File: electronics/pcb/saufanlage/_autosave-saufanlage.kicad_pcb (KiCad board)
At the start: 2 copper layers, 320.3 x 186.4 mm, 53 parts, among them J1 Conn_GND, J10 Conn_01x08_Male, J11 Conn_01x08_Male, J12 Conn_01x08_Male, J13 Conn_02x03_Odd_Even, J14 Conn_02x18_Odd_Even, J15 Conn_01x10_Male, J16 Conn_01x08_Male, J17 Conn_01x08_Male, J18 Conn_Finger, J19 Conn_Relais, J2 PJ-031D, J20 Conn_NFC, J21 Conn_Flow1, J22 Conn_Scale1, J23 Conn_01x15_Male, J24 Conn_01x15_Male, J25 Conn_Flow2, J26 Conn_Flow3, J27 Conn_Scale2, J28 Conn_Flow4, J29 Conn_01x15_Male, J3 Conn_3V3, J30 Conn_01x15_Male, J31 Conn_01x15_Male, J32 Conn_01x15_Male, J33 Conn_7SegmentI2C, J34 Conn_Scale3, J35 Conn_Scale4, J4 Conn_5V, J5 Conn_02x08_Odd_Even, J6 Conn_02x08_Odd_Even, J7 Conn_01x20_Male, J8 Raspberry_Pi_2_3, J9 Conn_01x20_Male

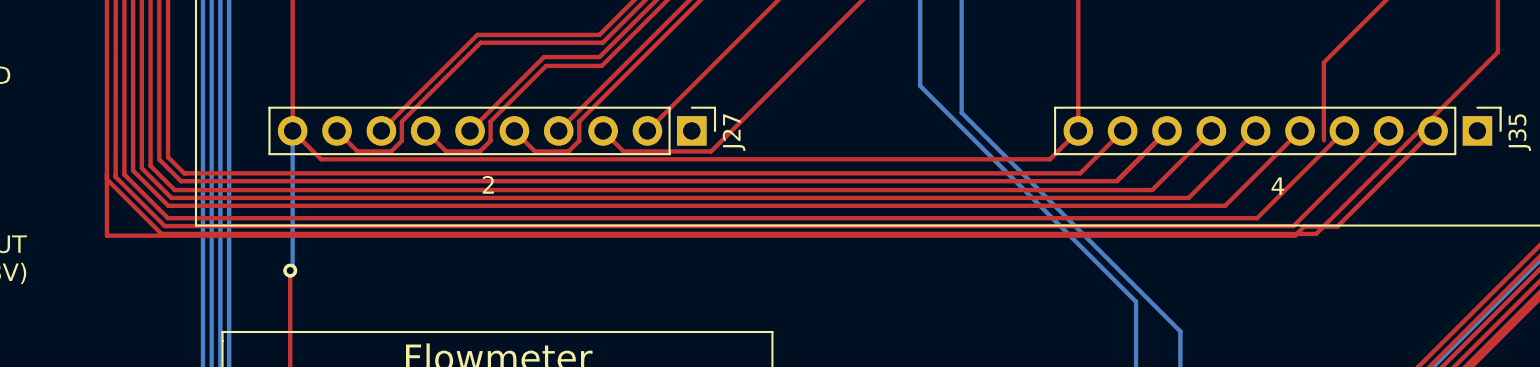
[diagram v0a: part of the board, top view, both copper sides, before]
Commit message: Add temperature sensors
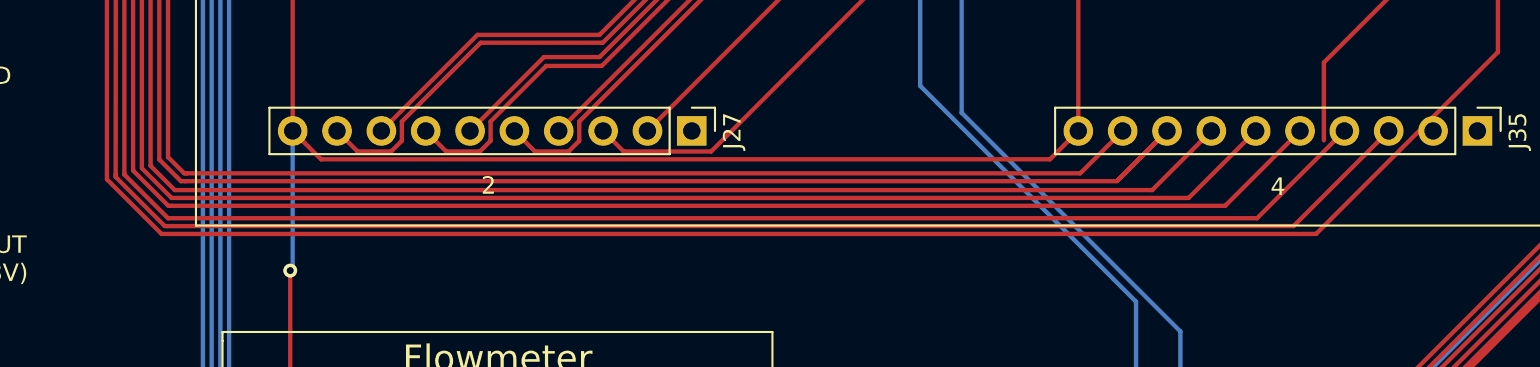
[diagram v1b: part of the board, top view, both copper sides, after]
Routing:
- net Sc4_SCK1: track 325.0 -> 243.1 mm
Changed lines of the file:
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@@
     (thickness 1.6)
     (drawings 313)
-    (tracks 1174)
+    (tracks 1169)
     (zones 0)
     (modules 53)
@@
   (segment (start 106 79.6) (end 117.58 68.02) (width 0.25) (layer F.Cu) (net 177) (status 20))
   (segment (start 96.5 115) (end 106 105.5) (width 0.25) (layer F.Cu) (net 177))
-  (segment (start 164.55641 186) (end 96.5 186) (width 0.25) (layer F.Cu) (net 177))
-  (segment (start 165.07641 185.48) (end 164.55641 186) (width 0.25) (layer F.Cu) (net 177))
-  (segment (start 166.98 185.48) (end 165.07641 185.48) (width 0.25) (layer F.Cu) (net 177))
-  (segment (start 166.98 185.48) (end 172.46 180) (width 0.25) (layer F.Cu) (net 177) (status 20))
   (segment (start 166.204999 176.080003) (end 166.204999 180.538591) (width 0.25) (layer F.Cu) (net 177))
   (segment (start 176.175001 175.484001) (end 176.175001 166.110001) (width 0.25) (layer F.Cu) (net 177))
@@
   (segment (start 96.5 182.77282) (end 99.627197 185.900017) (width 0.25) (layer F.Cu) (net 177))
   (segment (start 96.5 182.5) (end 96.5 182.77282) (width 0.25) (layer F.Cu) (net 177))
-  (segment (start 96.5 186) (end 96.5 182.5) (width 0.25) (layer F.Cu) (net 177))
   (segment (start 99.627197 185.900017) (end 165.758985 185.900017) (width 0.25) (layer F.Cu) (net 177))
   (segment (start 96.5 182.5) (end 96.5 115) (width 0.25) (layer F.Cu) (net 177))
